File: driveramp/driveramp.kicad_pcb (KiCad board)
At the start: 2 copper layers, 109 x 79 mm, 90 parts, among them J1 SMA, J2 SMA, K1 CONN_3, K2 CONN_3, P2 CONN_2, Q1 BC547BTA, T1 MABACT0067, T2 2x Fair-Rite 2843006802, coax, U1 DG9411, U2 MRFE6VP100H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

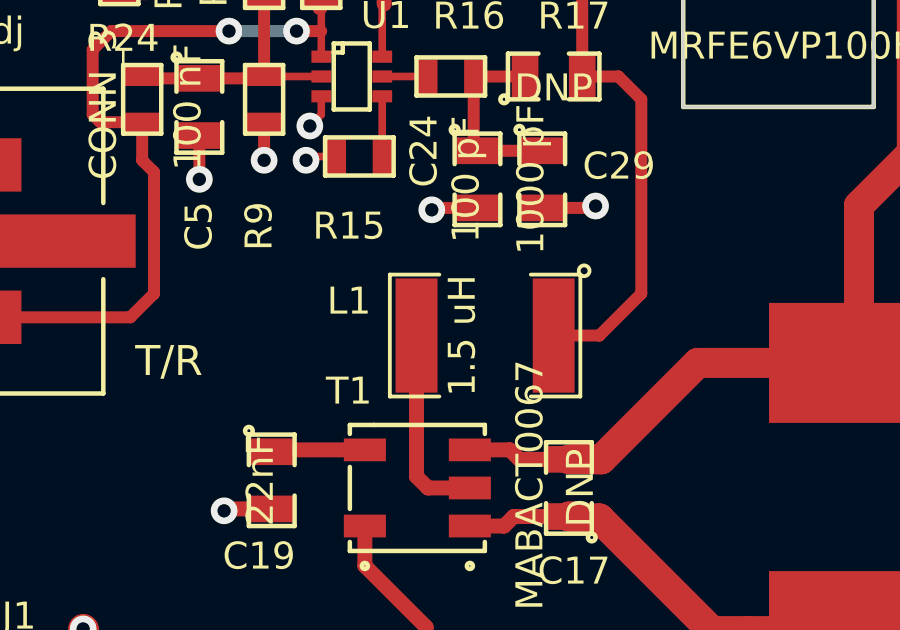
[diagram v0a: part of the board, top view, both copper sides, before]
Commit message: added missing cap on rf gnd of input transformer-balun..
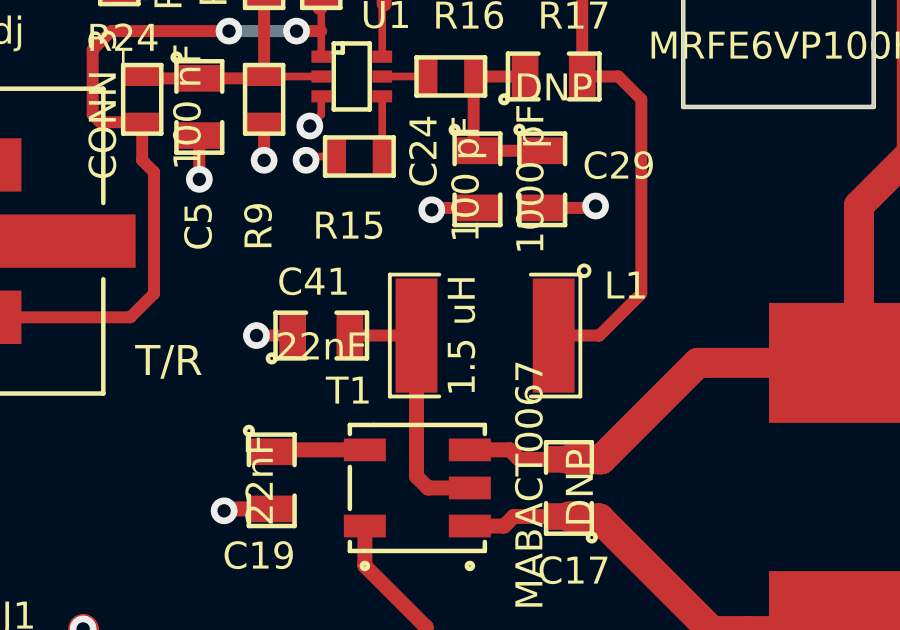
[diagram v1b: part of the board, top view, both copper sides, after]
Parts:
- added C41: 22nF, SMD_Packages:SMD-0805, F.Cu at (92.1, 104.6)
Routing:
- net Net-(C41-Pad2): track 6.63 -> 8.86 mm
- net GND: track 234.7 -> 236.3 mm, vias 102 -> 103

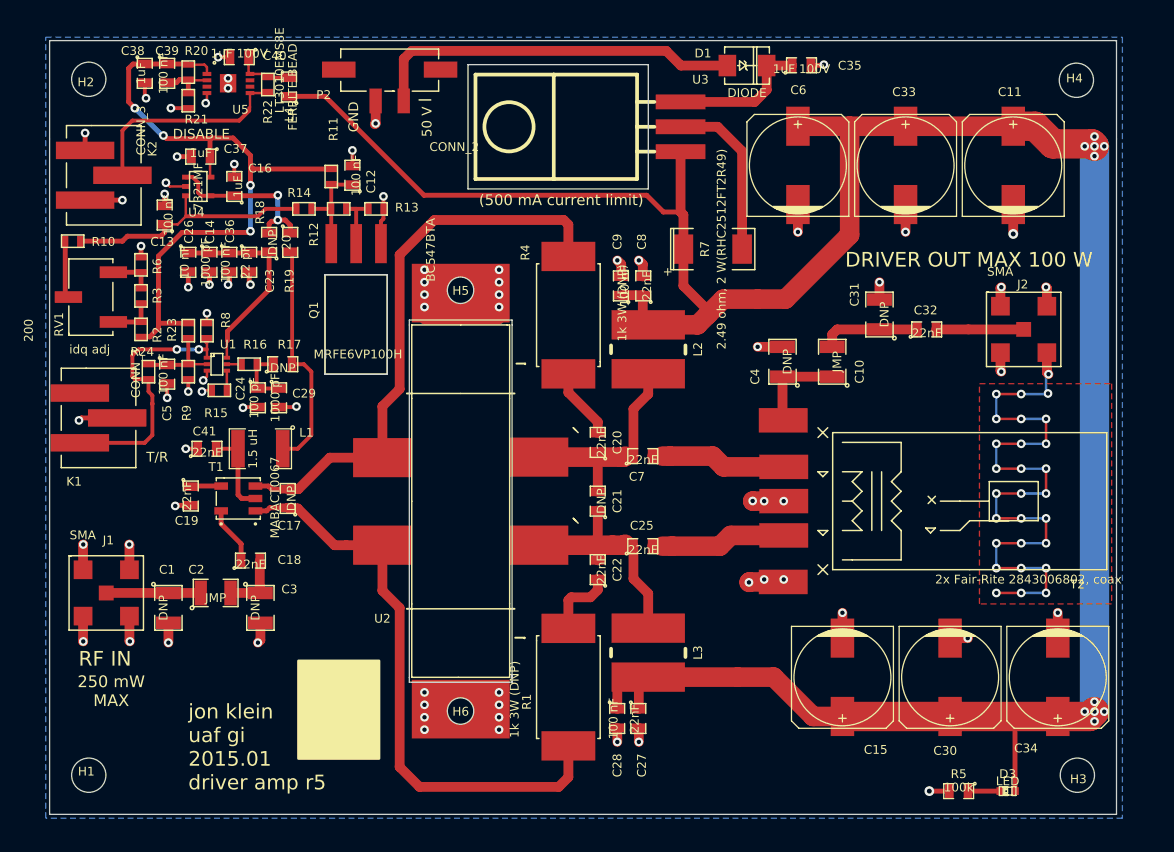
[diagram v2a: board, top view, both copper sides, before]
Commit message: finished layout of DFM'ed driver ampifier board.. except still need to change connectors
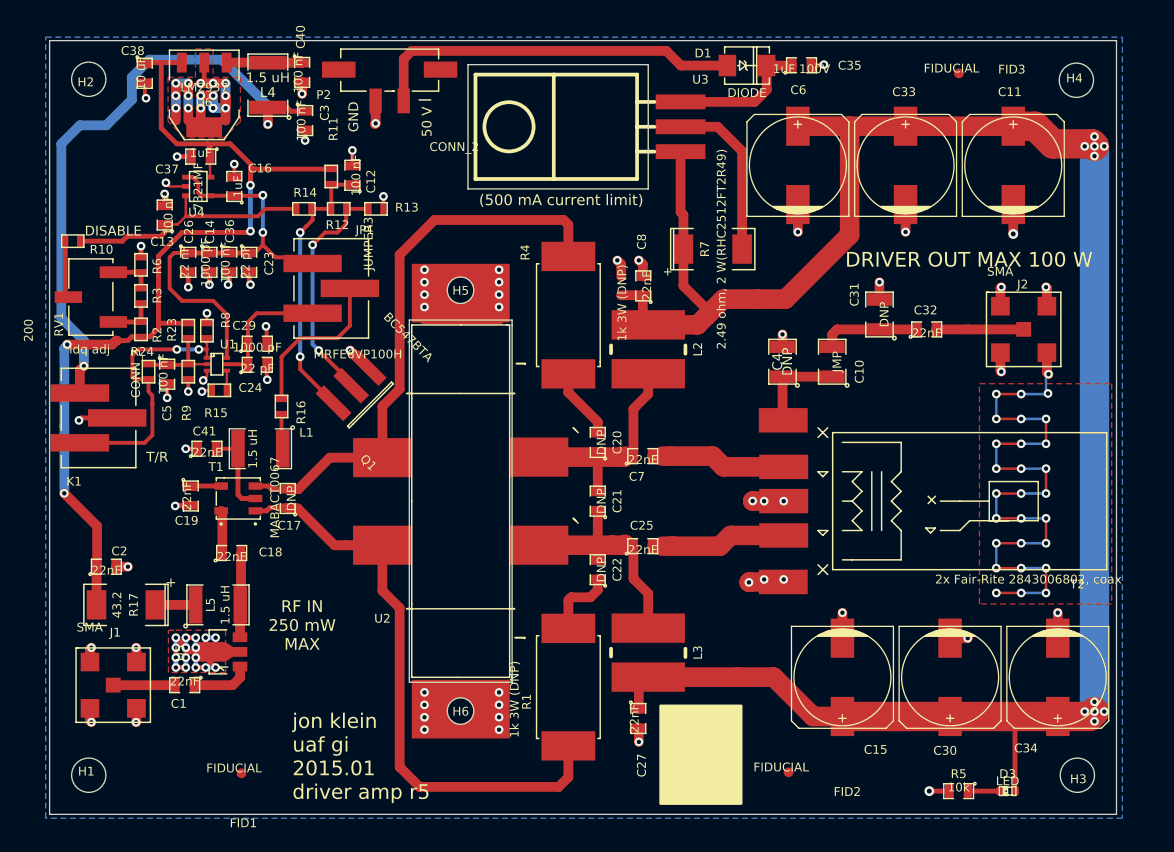
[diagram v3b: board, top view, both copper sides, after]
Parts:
- removed C28, C39, C9: 100 nF, SMD_Packages:SMD-0805
- removed K2: CONN_3, localconn:3-647166-3
- removed R18: DNP, SMD_Packages:SMD-0805
- removed R19: 20, SMD_Packages:SMD-0805
- removed R20: 52.3K 1%, SMD_Packages:SMD-0603
- removed R21: 10K 1%, SMD_Packages:SMD-0603
- removed R22: 10k, SMD_Packages:SMD-0603
- added FID1: FIDUCIAL, sdtransmitter:FID_1MM, F.Cu at (95.6, 137.8)
- added FID2: FIDUCIAL, sdtransmitter:FID_1MM, F.Cu at (151.5, 137.7)
- added FID3: FIDUCIAL, sdtransmitter:FID_1MM, F.Cu at (168.9, 66.3)
- added JP1: JUMPER3, localconn:3-647166-3, F.Cu at (104.8, 88.3)
- added L5: 1.5 uH, SMD_Packages:SMD-1812, F.Cu at (93.2, 120.6)
- added U6: LM2937, SMD_Packages:SOT-223, F.Cu at (91.8, 68.5)
- C1: value DNP -> 22nF; footprint SMD_Packages:SMD-1210 -> SMD_Packages:SMD-0805
- C2: value JMP -> 22nF; footprint SMD_Packages:SMD-1210 -> SMD_Packages:SMD-0805
- C20, C22: value 22nF -> DNP
- C24: value 100 pF -> 22 pF
- C26: value 10 nF -> 22 nF
- C3: value DNP -> 100 nF; footprint SMD_Packages:SMD-1210 -> SMD_Packages:SMD-0805
- C38: value 1uF -> 10 uF
- C40: value 1uF 100V -> 100 nF
- L4: value FERRITE BEAD -> 1.5 uH; footprint SMD_Packages:SMD-0805 -> SMD_Packages:SMD-1812
- R14: value 10k 1% -> 10k
- R15: value 1.5 -> 5.1
- R17: value DNP -> 43.2; footprint SMD_Packages:SMD-0805 -> SMD_Packages:SMD-2512_Pol
- R5: value 100k -> 10k
- U5: value LT3010EMS8E -> GALI6+; footprint local:MSOP8-EP -> Housings_SOT-89:SOT89-3_Housing
- moved U5 58.1 mm to (93.6, 125.4), turned to 90 degrees
- moved C3 50.0 mm to (102.1, 71.1)
- moved R17 29.3 mm to (83.8, 120.6), turned to 180 degrees
- moved Q1 12.8 mm to (108.6, 96.4), turned to 315 degrees
- moved C2 11.5 mm to (81.8, 116.7)
- moved J1 9.45 mm to (82.5, 128.8)
- moved C1 8.07 mm to (89.8, 128.8), turned to 180 degrees
- moved C40 6.61 mm to (101.8, 66.2), turned to 270 degrees
- moved C29 5.95 mm to (97.2, 93.9), turned to 0 degrees
- moved R16 5.44 mm to (99.7, 100.3), turned to 90 degrees
- moved C24 3.37 mm to (97.2, 96.1), turned to 0 degrees
- moved L4 2.17 mm to (98.3, 67.5)
- moved C18 2.07 mm to (94.6, 115.3)
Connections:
- C1 pad 2: GND -> Net-(C1-Pad2)
- C16 pad 1: Net-(C16-Pad1) -> Net-(C14-Pad1)
- C2 pad 1: Net-(C1-Pad1) -> +8V
- C2 pad 2: Net-(C18-Pad2) -> GND
- C3 pad 1: Net-(C18-Pad2) -> VPP
- J1 pad 1: Net-(C1-Pad1) -> Net-(C1-Pad2)
- K1 pad 1: (no net) -> VPP
- L4 pad 1: VDD -> VPP
- R16 pad 1: Net-(C24-Pad1) -> Net-(L1-Pad1)
- R16 pad 2: Net-(R16-Pad2) -> Net-(JP1-Pad2)
- R17 pad 1: Net-(C24-Pad1) -> Net-(L5-Pad1)
- R17 pad 2: Net-(L1-Pad1) -> +8V
- U1 pad 5: Net-(R16-Pad2) -> Net-(C24-Pad1)
- U4 pad 1: Net-(C16-Pad1) -> Net-(C14-Pad1)
- U4 pad 4: Net-(C16-Pad1) -> Net-(C14-Pad1)
- U5 pad 1: +8V -> Net-(C1-Pad1)
- U5 pad 2: Net-(C39-Pad2) -> GND
- U5 pad 3: (no net) -> Net-(C18-Pad2)
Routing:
- net VPP: track 0.00 -> 62.1 mm, vias 0 -> 2
- net VDD: track 273.6 -> 224.6 mm
- net +8V: track 70.4 -> 99.5 mm
- net GND: track 236.3 -> 264.3 mm, vias 103 -> 127
- net Net-(C14-Pad1): track 20.9 -> 44.8 mm, vias 0 -> 2
- net Net-(K2-Pad2): track 22.1 -> 0.00 mm
- net Net-(L1-Pad1): track 23.8 -> 3.61 mm
- net Net-(C12-Pad1): track 10.3 -> 28.7 mm, vias 0 -> 2
- net Net-(C16-Pad1): track 17.7 -> 0.00 mm, vias 2 -> 0
- net Net-(Q1-Pad2): track 6.86 -> 24.1 mm, vias 0 -> 2
- net Net-(JP1-Pad2): track 0.00 -> 16.4 mm
- net Net-(C24-Pad1): track 6.40 -> 13.5 mm
- net Net-(C1-Pad2): track 0.00 -> 6.35 mm
- net Net-(C39-Pad2): track 5.63 -> 0.00 mm
- net Net-(L5-Pad1): track 0.00 -> 4.11 mm
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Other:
- outline, holes or cut-outs redrawn
- board text added: "RF IN 250 mW MAX"
- board text removed: "250 mW MAX"
- board text removed: "RF IN"
